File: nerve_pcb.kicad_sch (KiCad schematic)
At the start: 46 parts, among them J1 TC2050-IDC, J2 2171750001, J4 472192001, J5 2x8, J6 2x15, SW1 SPST, SW2 SPST, U1 ld39150dt33-r, U2 STM32F446RET, Y1 8M, Y2 32k768

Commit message: Revert to 603 package sizes and add WIP PCB
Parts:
- C1, C10, C11, C12, C13, C2, C3, C4, C5, C6, C7, C8, C9: footprint Capacitor_SMD:C_0402_1005Metric -> Capacitor_SMD:C_0603_1608Metric
- R11, R12, R13, R4, R5, R6, R7, R8: footprint Resistor_SMD:R_0402_1005Metric -> Resistor_SMD:R_0603_1608Metric
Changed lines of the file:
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@@
 			)
 		)
-		(property "Footprint" "Capacitor_SMD:C_0402_1005Metric"
+		(property "Footprint" "Capacitor_SMD:C_0603_1608Metric"
 			(at 277.8252 35.56 0)
 			(effects
@@
 			)
 		)
-		(property "Footprint" "Capacitor_SMD:C_0402_1005Metric"
+		(property "Footprint" "Capacitor_SMD:C_0603_1608Metric"
 			(at 252.4252 35.56 0)
 			(effects
@@
 			)
 		)
-		(property "Footprint" "Resistor_SMD:R_0402_1005Metric"
+		(property "Footprint" "Resistor_SMD:R_0603_1608Metric"
 			(at 23.622 99.06 90)
 			(effects
@@
 			)
 		)
-		(property "Footprint" "Resistor_SMD:R_0402_1005Metric"
+		(property "Footprint" "Resistor_SMD:R_0603_1608Metric"
 			(at 229.362 78.74 90)
 			(effects
@@
 			)
 		)
-		(property "Footprint" "Capacitor_SMD:C_0402_1005Metric"
+		(property "Footprint" "Capacitor_SMD:C_0603_1608Metric"
 			(at 39.0652 113.03 0)
 			(effects
@@
 			)
 		)
-		(property "Footprint" "Capacitor_SMD:C_0402_1005Metric"
+		(property "Footprint" "Capacitor_SMD:C_0603_1608Metric"
 			(at 133.0452 53.34 0)
 			(effects
@@
 			)
 		)
-		(property "Footprint" "Resistor_SMD:R_0402_1005Metric"
+		(property "Footprint" "Resistor_SMD:R_0603_1608Metric"
 			(at 224.282 78.74 90)
 			(effects
@@
 			)
 		)
-		(property "Footprint" "Capacitor_SMD:C_0402_1005Metric"
+		(property "Footprint" "Capacitor_SMD:C_0603_1608Metric"
 			(at 58.7248 153.67 0)
 			(effects
@@
 			)
 		)
-		(property "Footprint" "Capacitor_SMD:C_0402_1005Metric"
+		(property "Footprint" "Capacitor_SMD:C_0603_1608Metric"
 			(at 107.6452 53.34 0)
 			(effects
@@
 			)
 		)
-		(property "Footprint" "Resistor_SMD:R_0402_1005Metric"
+		(property "Footprint" "Resistor_SMD:R_0603_1608Metric"
 			(at 221.742 78.74 90)
 			(effects
@@
 			)
 		)
-		(property "Footprint" "Resistor_SMD:R_0402_1005Metric"
+		(property "Footprint" "Resistor_SMD:R_0603_1608Metric"
 			(at 42.672 146.05 90)
 			(effects
@@
 			)
 		)
-		(property "Footprint" "Capacitor_SMD:C_0402_1005Metric"
+		(property "Footprint" "Capacitor_SMD:C_0603_1608Metric"
 			(at 82.2452 53.34 0)
 			(effects
@@
 			)
 		)
-		(property "Footprint" "Capacitor_SMD:C_0402_1005Metric"
+		(property "Footprint" "Capacitor_SMD:C_0603_1608Metric"
 			(at 120.3452 53.34 0)
 			(effects
@@
 			)
 		)
-		(property "Footprint" "Capacitor_SMD:C_0402_1005Metric"
+		(property "Footprint" "Capacitor_SMD:C_0603_1608Metric"
 			(at 94.9452 53.34 0)
 			(effects
@@
 			)
 		)
-		(property "Footprint" "Capacitor_SMD:C_0402_1005Metric"
+		(property "Footprint" "Capacitor_SMD:C_0603_1608Metric"
 			(at 51.7652 67.31 0)
 			(effects
@@
 			)
 		)
-		(property "Footprint" "Capacitor_SMD:C_0402_1005Metric"
+		(property "Footprint" "Capacitor_SMD:C_0603_1608Metric"
 			(at 70.8152 33.02 0)
 			(effects
@@
 			)
 		)
-		(property "Footprint" "Resistor_SMD:R_0402_1005Metric"
+		(property "Footprint" "Resistor_SMD:R_0603_1608Metric"
 			(at 219.202 78.74 90)
 			(effects
@@
 			)
 		)
-		(property "Footprint" "Capacitor_SMD:C_0402_1005Metric"
+		(property "Footprint" "Capacitor_SMD:C_0603_1608Metric"
 			(at 62.5348 33.02 0)
 			(effects
@@
 			)
 		)
-		(property "Footprint" "Resistor_SMD:R_0402_1005Metric"
+		(property "Footprint" "Resistor_SMD:R_0603_1608Metric"
 			(at 226.822 78.74 90)
 			(effects
@@
 			)
 		)
-		(property "Footprint" "Resistor_SMD:R_0402_1005Metric"
+		(property "Footprint" "Resistor_SMD:R_0603_1608Metric"
 			(at 29.972 146.05 90)
 			(effects
@@
 			)
 		)
-		(property "Footprint" "Capacitor_SMD:C_0402_1005Metric"
+		(property "Footprint" "Capacitor_SMD:C_0603_1608Metric"
 			(at 26.3652 113.03 0)
 			(effects

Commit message: Swap to 1.27mm board-to-board and WIP PCB
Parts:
- J5: footprint Connector_PinSocket_2.54mm:PinSocket_2x08_P2.54mm_Vertical_SMD -> Connector_PinSocket_1.27mm:PinSocket_2x08_P1.27mm_Vertical_SMD
- J6: footprint Connector_PinSocket_2.54mm:PinSocket_2x15_P2.54mm_Vertical_SMD -> Connector_PinSocket_1.27mm:PinSocket_2x15_P1.27mm_Vertical_SMD
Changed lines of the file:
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@@
 			)
 		)
-		(property "Footprint" "Connector_PinSocket_2.54mm:PinSocket_2x08_P2.54mm_Vertical_SMD"
+		(property "Footprint" "Connector_PinSocket_1.27mm:PinSocket_2x08_P1.27mm_Vertical_SMD"
 			(at 195.58 129.54 0)
 			(effects
@@
 			)
 		)
-		(property "Footprint" "Connector_PinSocket_2.54mm:PinSocket_2x15_P2.54mm_Vertical_SMD"
+		(property "Footprint" "Connector_PinSocket_1.27mm:PinSocket_2x15_P1.27mm_Vertical_SMD"
 			(at 246.38 139.7 0)
 			(effects

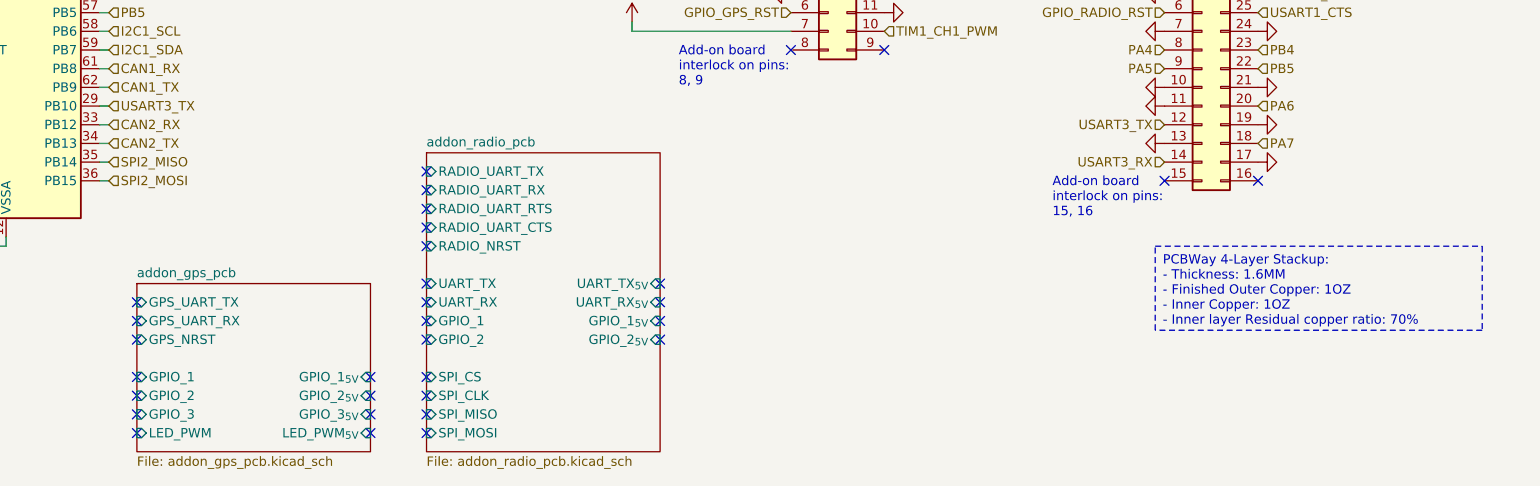
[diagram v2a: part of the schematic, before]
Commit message: Split and remove add-on board designs
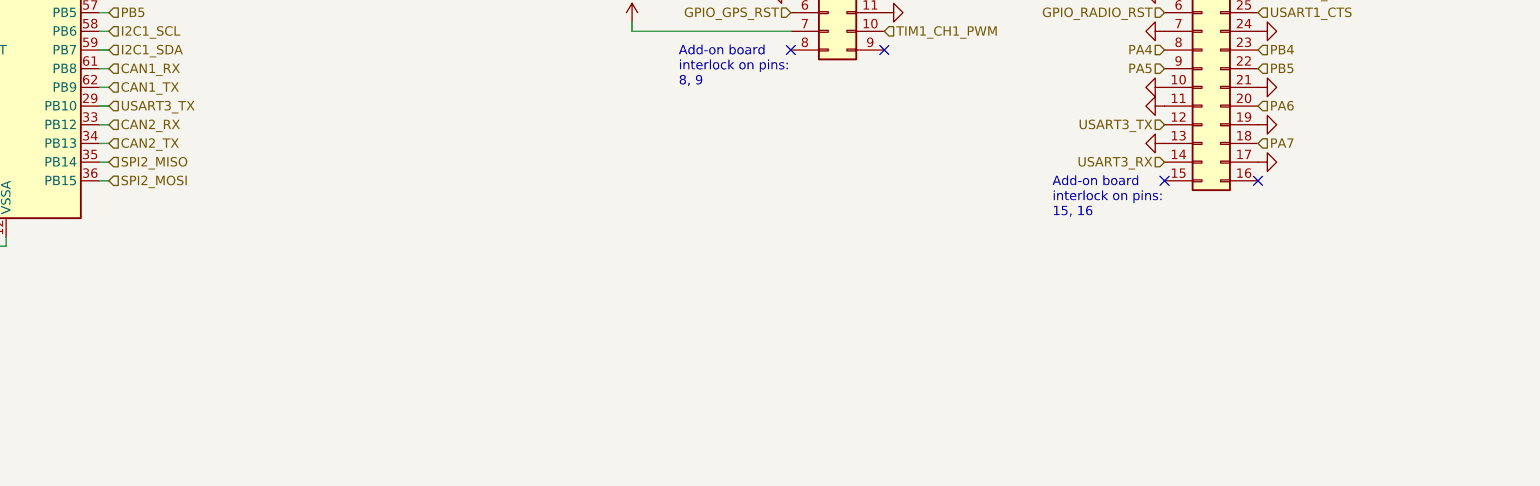
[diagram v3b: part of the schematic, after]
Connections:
- no-connect marks 34 -> 6
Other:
- removed sheet addon_gps_pcb
- removed sheet addon_radio_pcb

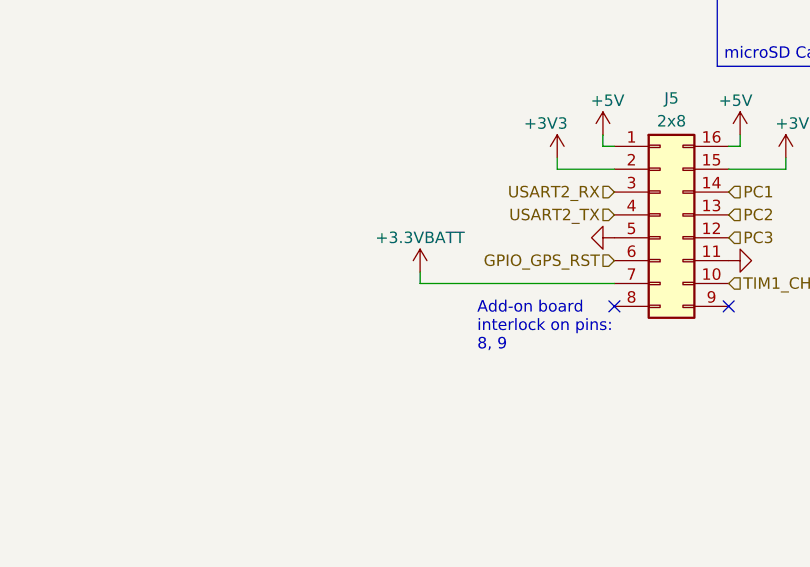
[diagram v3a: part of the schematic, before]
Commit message: Add missing power flag
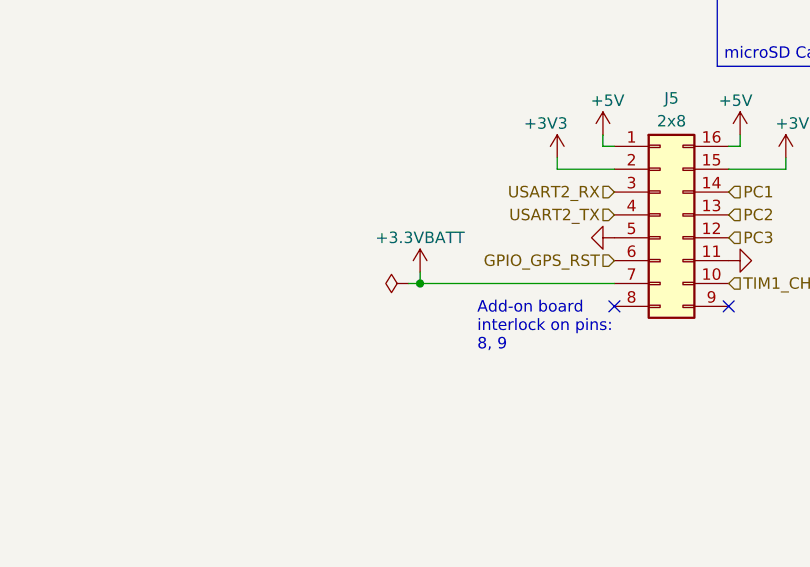
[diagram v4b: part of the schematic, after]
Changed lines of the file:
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@@
 	)
 	(junction
+		(at 168.91 137.16)
+		(diameter 0)
+		(color 0 0 0 0)
+	)
+	(junction
 		(at 93.98 44.45)
 		(diameter 0)
@@
 	(wire
 		(pts
+			(xy 167.64 137.16) (xy 168.91 137.16)
+		)
+		(stroke
+			(width 0)
+			(type default)
+		)
+	)
+	(wire
+		(pts
 			(xy 73.66 166.37) (xy 76.2 166.37)
 		)
@@
 					(unit 1)
 				)
+			)
+		)
+	)
+	(symbol
+		(lib_id "power:PWR_FLAG")
+		(at 167.64 137.16 90)
+		(unit 1)
+		(exclude_from_sim no)
+		(in_bom yes)
+		(on_board yes)
+		(dnp no)
+		(property "Reference" "#FLG04"
+			(at 165.735 137.16 0)
+			(effects
+				(font
+					(size 1.27 1.27)
+				)
+				(hide yes)
+			)
+		)
+		(property "Value" "PWR_FLAG"
+			(at 163.576 137.16 0)
+			(effects
+				(font
+					(size 1.27 1.27)
+				)
+				(hide yes)
+			)
+		)
+		(property "Footprint" ""
+			(at 167.64 137.16 0)
+			(effects
+				(font
+					(size 1.27 1.27)
+				)
+				(hide yes)
+			)
+		)
+		(property "Datasheet" "~"
+			(at 167.64 137.16 0)
+			(effects
+				(font
+					(size 1.27 1.27)
+				)
+				(hide yes)
+			)
+		)
+		(property "Description" "Special symbol for telling ERC where power comes from"
+			(at 167.64 137.16 0)
+			(effects
+				(font
+					(size 1.27 1.27)
+				)
+				(hide yes)
+			)
+		)
+		(pin "1"
+		)
+		(instances
+			(project "nerve_pcb"
+				(path "/c0277862-b3f2-4e0e-986f-34702f0543f0"
+					(reference "#FLG04")
+					(unit 1)
+				)

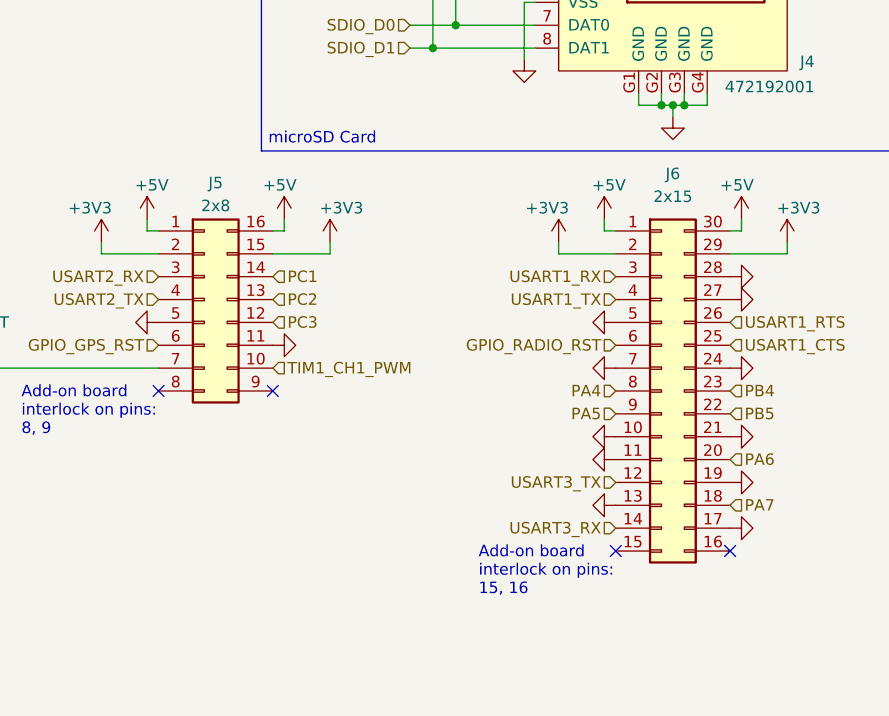
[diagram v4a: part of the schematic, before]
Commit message: Fix board-to-board connector pinout
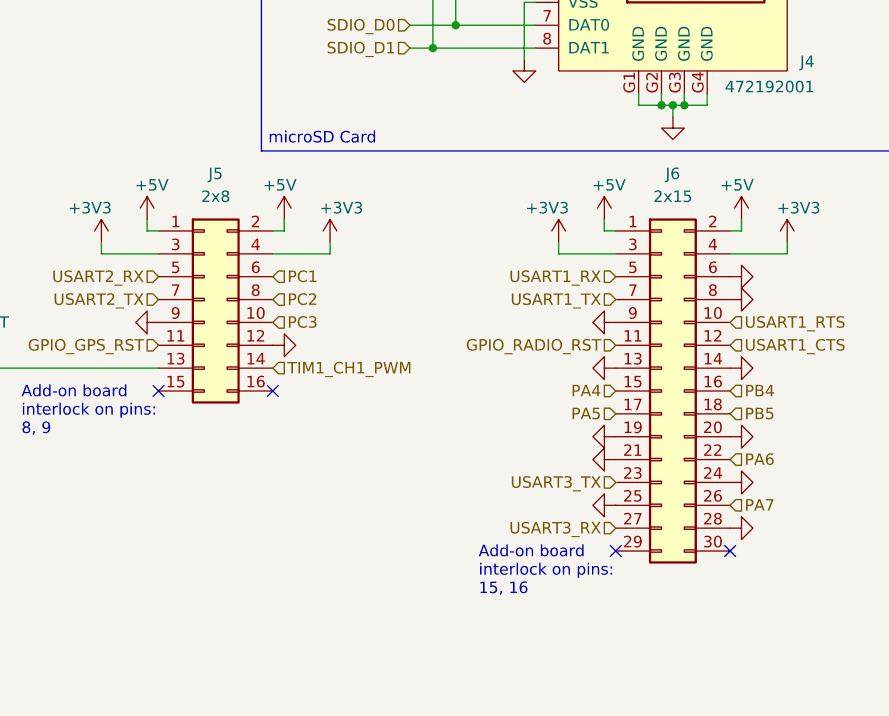
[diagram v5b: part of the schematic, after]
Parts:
- removed J5: 2x8, Connector_PinSocket_1.27mm:PinSocket_2x08_P1.27mm_Vertical_SMD, symbol Connector_Generic:Conn_02x08_Counter_Clockwise
- removed J6: 2x15, Connector_PinSocket_1.27mm:PinSocket_2x15_P1.27mm_Vertical_SMD, symbol Connector_Generic:Conn_02x15_Counter_Clockwise
- added J5: 2x8, Connector_PinSocket_1.27mm:PinSocket_2x08_P1.27mm_Vertical_SMD, symbol Connector_Generic:Conn_02x08_Odd_Even
- added J6: 2x15, Connector_PinSocket_1.27mm:PinSocket_2x15_P1.27mm_Vertical_SMD, symbol Connector_Generic:Conn_02x15_Odd_Even
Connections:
- net +3.3VBATT: now also J5.13 (Pin_13)
- net +3V3: now also J5.3 (Pin_3), J5.4 (Pin_4), J6.3 (Pin_3), J6.4 (Pin_4)
- net +5V: now also J5.1 (Pin_1), J5.2 (Pin_2), J6.1 (Pin_1), J6.2 (Pin_2)
- net GND: now also J5.12 (Pin_12), J5.9 (Pin_9), J6.13 (Pin_13), J6.14 (Pin_14), J6.19 (Pin_19), J6.20 (Pin_20), J6.21 (Pin_21), J6.24 (Pin_24), J6.25 (Pin_25), J6.28 (Pin_28), J6.6 (Pin_6), J6.8 (Pin_8), J6.9 (Pin_9)
- net GPIO_GPS_RST: now also J5.11 (Pin_11)
- net GPIO_RADIO_RST: now also J6.11 (Pin_11)
- net PA4: now also J6.15 (Pin_15)
- net PA5: now also J6.17 (Pin_17)
- net PA6: now also J6.22 (Pin_22)
- net PA7: now also J6.26 (Pin_26)
- net PB4: now also J6.16 (Pin_16)
- net PB5: now also J6.18 (Pin_18)
- net PC1: now also J5.6 (Pin_6)
- net PC2: now also J5.8 (Pin_8)
- net PC3: now also J5.10 (Pin_10)
- net TIM1_CH1_PWM: now also J5.14 (Pin_14)
- net USART1_CTS: now also J6.12 (Pin_12)
- net USART1_RTS: now also J6.10 (Pin_10)
- net USART1_RX: now also J6.5 (Pin_5)
- net USART1_TX: now also J6.7 (Pin_7)
- net USART2_RX: now also J5.5 (Pin_5)
- net USART2_TX: now also J5.7 (Pin_7)
- net USART3_RX: now also J6.27 (Pin_27)
- net USART3_TX: now also J6.23 (Pin_23)
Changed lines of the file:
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@@
 	)
 	(symbol
+		(lib_id "Connector_Generic:Conn_02x15_Odd_Even")
+		(at 246.38 139.7 0)
+		(unit 1)
+		(exclude_from_sim no)
+		(in_bom yes)
+		(on_board yes)
+		(dnp no)
+		(fields_autoplaced yes)
+		(property "Reference" "J6"
+			(at 247.65 115.57 0)
+			(effects
+				(font
+					(size 1.27 1.27)
+				)
+			)
+		)
+		(property "Value" "2x15"
+			(at 247.65 118.11 0)
+			(effects
+				(font
+					(size 1.27 1.27)
+				)
+			)
+		)
+		(property "Footprint" "Connector_PinSocket_1.27mm:PinSocket_2x15_P1.27mm_Vertical_SMD"
+			(at 246.38 139.7 0)
+			(effects
+				(font
+					(size 1.27 1.27)
+				)
+				(hide yes)
+			)
+		)
+		(property "Datasheet" "~"
+			(at 246.38 139.7 0)
+			(effects
+				(font
+					(size 1.27 1.27)
+				)
+				(hide yes)
+			)
+		)
+		(property "Description" "Generic connector, double row, 02x15, odd/even pin numbering scheme (row 1 odd numbers, row 2 even numbers), script generated (kicad-library-utils/schlib/autogen/connector/)"
+			(at 246.38 139.7 0)
+			(effects
+				(font
+					(size 1.27 1.27)
+				)
+				(hide yes)
+			)
+		)
+		(pin "23"
+		)
+		(pin "2"
+		)
+		(pin "20"
+		)
+		(pin "28"
+		)
+		(pin "12"
+		)
+		(pin "22"
+		)
+		(pin "3"
+		)
+		(pin "4"
+		)
+		(pin "1"
+		)
+		(pin "14"
+		)
+		(pin "11"
+		)
+		(pin "7"
+		)
+		(pin "30"
+		)
+		(pin "13"
+		)
+		(pin "21"
+		)
+		(pin "6"
+		)
+		(pin "25"
+		)
+		(pin "19"
+		)
+		(pin "24"
+		)
+		(pin "27"
+		)
+		(pin "29"
+		)
+		(pin "16"
+		)
+		(pin "5"
+		)
+		(pin "15"
+		)
+		(pin "8"
+		)
+		(pin "17"
+		)
+		(pin "10"
+		)
+		(pin "18"
+		)
+		(pin "9"
+		)
+		(pin "26"
+		)
+		(instances
+			(project ""
+				(path "/c0277862-b3f2-4e0e-986f-34702f0543f0"
+					(reference "J6")
+					(unit 1)
+				)
+			)
+		)
+	)
+	(symbol
 		(lib_id "Device:C")
 		(at 251.46 31.75 0)
@@
 	)
 	(symbol
+		(lib_id "Connector_Generic:Conn_02x08_Odd_Even")
+		(at 195.58 129.54 0)
+		(unit 1)
+		(exclude_from_sim no)
+		(in_bom yes)
+		(on_board yes)
+		(dnp no)
+		(fields_autoplaced yes)
+		(property "Reference" "J5"
+			(at 196.85 115.57 0)
+			(effects
+				(font
+					(size 1.27 1.27)
+				)
+			)
+		)
+		(property "Value" "2x8"
+			(at 196.85 118.11 0)
+			(effects
+				(font
+					(size 1.27 1.27)
+				)
+			)
+		)
+		(property "Footprint" "Connector_PinSocket_1.27mm:PinSocket_2x08_P1.27mm_Vertical_SMD"
+			(at 195.58 129.54 0)
+			(effects
+				(font
+					(size 1.27 1.27)
+				)
+				(hide yes)
+			)
+		)
+		(property "Datasheet" "~"
+			(at 195.58 129.54 0)
+			(effects
+				(font
+					(size 1.27 1.27)
+				)
+				(hide yes)
+			)
+		)
+		(property "Description" "Generic connector, double row, 02x08, odd/even pin numbering scheme (row 1 odd numbers, row 2 even numbers), script generated (kicad-library-utils/schlib/autogen/connector/)"
+			(at 195.58 129.54 0)
+			(effects
+				(font
+					(size 1.27 1.27)
+				)
+				(hide yes)
+			)
+		)
+		(pin "1"
+		)
+		(pin "3"
+		)
+		(pin "7"
+		)
+		(pin "4"
+		)
+		(pin "13"
+		)
+		(pin "14"
+		)
+		(pin "2"
+		)
+		(pin "10"
+		)
+		(pin "6"
+		)
+		(pin "8"
+		)
+		(pin "15"
+		)
+		(pin "11"
+		)
+		(pin "12"
+		)
+		(pin "9"
+		)
+		(pin "5"
+		)
+		(pin "16"
+		)
+		(instances
+			(project ""
+				(path "/c0277862-b3f2-4e0e-986f-34702f0543f0"
+					(reference "J5")
+					(unit 1)
+				)
+			)
+		)
+	)
+	(symbol
 		(lib_id "Device:R")
 		(at 231.14 78.74 0)
@@
 	)
 	(symbol
-		(lib_id "Connector_Generic:Conn_02x08_Counter_Clockwise")
-		(at 195.58 129.54 0)
-		(unit 1)
-		(exclude_from_sim no)
-		(in_bom yes)
-		(on_board yes)
-		(dnp no)
-		(property "Reference" "J5"
-			(at 196.85 116.586 0)
-			(effects
-				(font
-					(size 1.27 1.27)
-				)
-			)
-		)
-		(property "Value" "2x8"
-			(at 196.85 119.126 0)
-			(effects
-				(font
-					(size 1.27 1.27)
-				)
-			)
-		)
-		(property "Footprint" "Connector_PinSocket_1.27mm:PinSocket_2x08_P1.27mm_Vertical_SMD"
-			(at 195.58 129.54 0)
-			(effects
-				(font
-					(size 1.27 1.27)
-				)
-				(hide yes)
-			)
-		)
-		(property "Datasheet" "~"
-			(at 195.58 129.54 0)
-			(effects
-				(font
-					(size 1.27 1.27)
-				)
-				(hide yes)
-			)
-		)
-		(property "Description" "Generic connector, double row, 02x08, counter clockwise pin numbering scheme (similar to DIP package numbering), script generated (kicad-library-utils/schlib/autogen/connector/)"
-			(at 195.58 129.54 0)
-			(effects
-				(font
-					(size 1.27 1.27)
-				)
-				(hide yes)
-			)
-		)
-		(pin "16"
-		)
-		(pin "10"
-		)
-		(pin "15"
-		)
-		(pin "7"
-		)
-		(pin "3"
-		)
-		(pin "4"
-		)
-		(pin "12"
-		)
-		(pin "6"
-		)
-		(pin "13"
-		)
-		(pin "14"
-		)
-		(pin "11"
-		)
-		(pin "8"
-		)
-		(pin "9"
-		)
-		(pin "5"
-		)
-		(pin "1"
-		)
-		(pin "2"
-		)
-		(instances
-			(project ""
-				(path "/c0277862-b3f2-4e0e-986f-34702f0543f0"
-					(reference "J5")
-					(unit 1)
-				)
-			)
-		)
-	)
-	(symbol
 		(lib_id "power:GND")
 		(at 78.74 167.64 0)
@@
 					(unit 1)
 				)
-			)
-		)
-	)
-	(symbol
-		(lib_id "Connector_Generic:Conn_02x15_Counter_Clockwise")
-		(at 246.38 139.7 0)
-		(unit 1)
-		(exclude_from_sim no)
-		(in_bom yes)
-		(on_board yes)
-		(dnp no)
-		(fields_autoplaced yes)
-		(property "Reference" "J6"
-			(at 247.65 115.57 0)
-			(effects
-				(font
-					(size 1.27 1.27)
-				)
-			)
-		)
-		(property "Value" "2x15"
-			(at 247.65 118.11 0)
-			(effects
-				(font
-					(size 1.27 1.27)
-				)
-			)
-		)
-		(property "Footprint" "Connector_PinSocket_1.27mm:PinSocket_2x15_P1.27mm_Vertical_SMD"
-			(at 246.38 139.7 0)
-			(effects
-				(font
-					(size 1.27 1.27)
-				)
-				(hide yes)
-			)
-		)
-		(property "Datasheet" "~"
-			(at 246.38 139.7 0)
-			(effects
-				(font
-					(size 1.27 1.27)
-				)
-				(hide yes)
-			)
-		)
-		(property "Description" "Generic connector, double row, 02x15, counter clockwise pin numbering scheme (similar to DIP package numbering), script generated (kicad-library-utils/schlib/autogen/connector/)"
-			(at 246.38 139.7 0)
-			(effects
-				(font
-					(size 1.27 1.27)
-				)
-				(hide yes)
-			)
-		)
-		(pin "21"
-		)
-		(pin "15"
-		)
-		(pin "16"
-		)
-		(pin "25"
-		)
-		(pin "19"
-		)
-		(pin "13"
-		)
-		(pin "2"
-		)
-		(pin "10"
-		)
-		(pin "27"
-		)
-		(pin "11"
-		)
-		(pin "28"
-		)
-		(pin "29"
-		)
-		(pin "24"
-		)
-		(pin "1"
-		)
-		(pin "3"
-		)
-		(pin "4"
-		)
-		(pin "30"
-		)
-		(pin "20"
-		)
-		(pin "6"
-		)
-		(pin "9"
-		)
-		(pin "26"
-		)
-		(pin "14"
-		)
-		(pin "5"
-		)
-		(pin "7"
-		)
-		(pin "12"
-		)
-		(pin "8"
-		)
-		(pin "17"
-		)
-		(pin "23"
-		)
-		(pin "18"
-		)
-		(pin "22"
-		)
-		(instances
-			(project "nerve_pcb"
-				(path "/c0277862-b3f2-4e0e-986f-34702f0543f0"
-					(reference "J6")
-					(unit 1)
-				)
